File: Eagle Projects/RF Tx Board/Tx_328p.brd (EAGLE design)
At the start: 216.8 x 165.1 mm, 46 parts, among them Q3 16MHz, Q4 16MHz, U1 ATMEGA328P_TQFP, U2 MCP2551

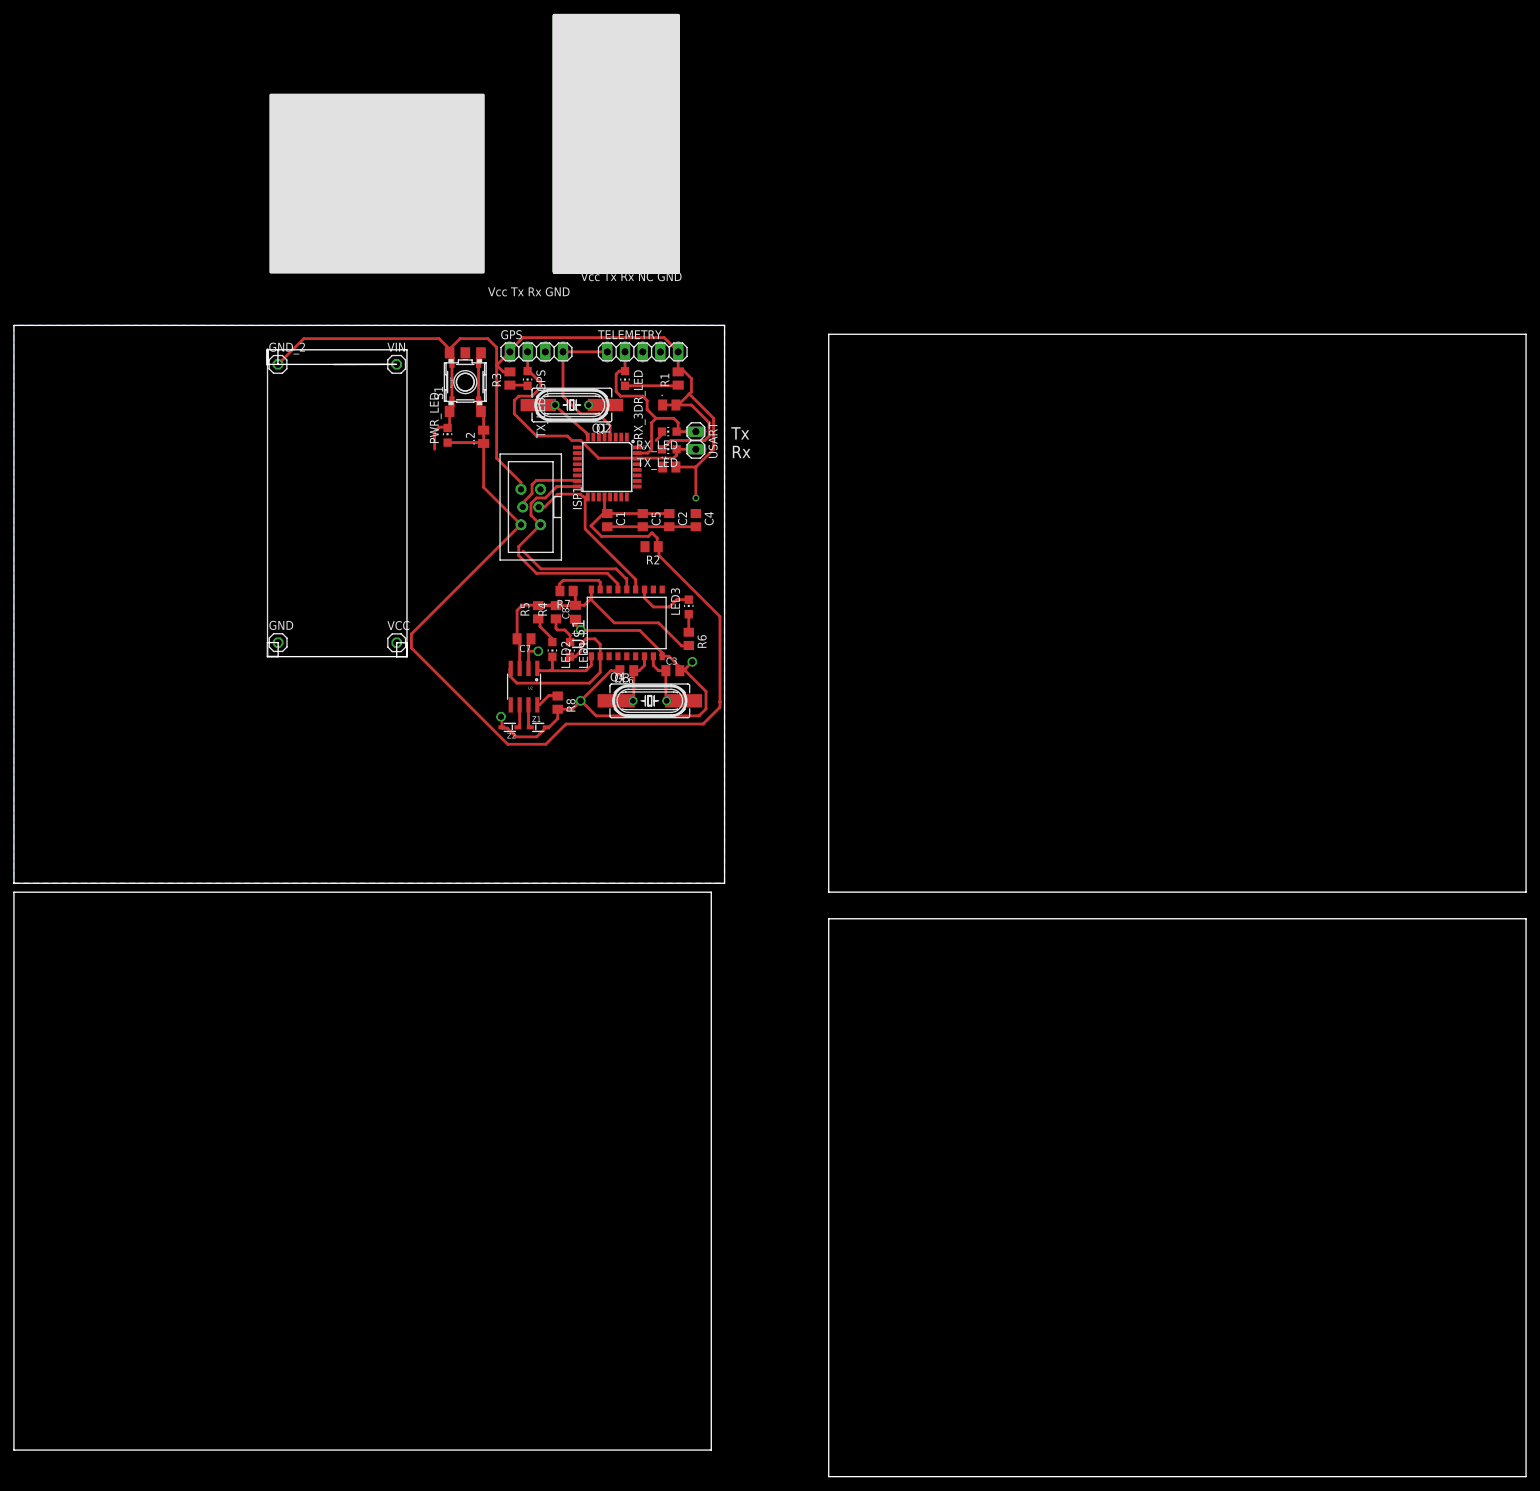
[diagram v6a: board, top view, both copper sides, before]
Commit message: Tidy up both boards
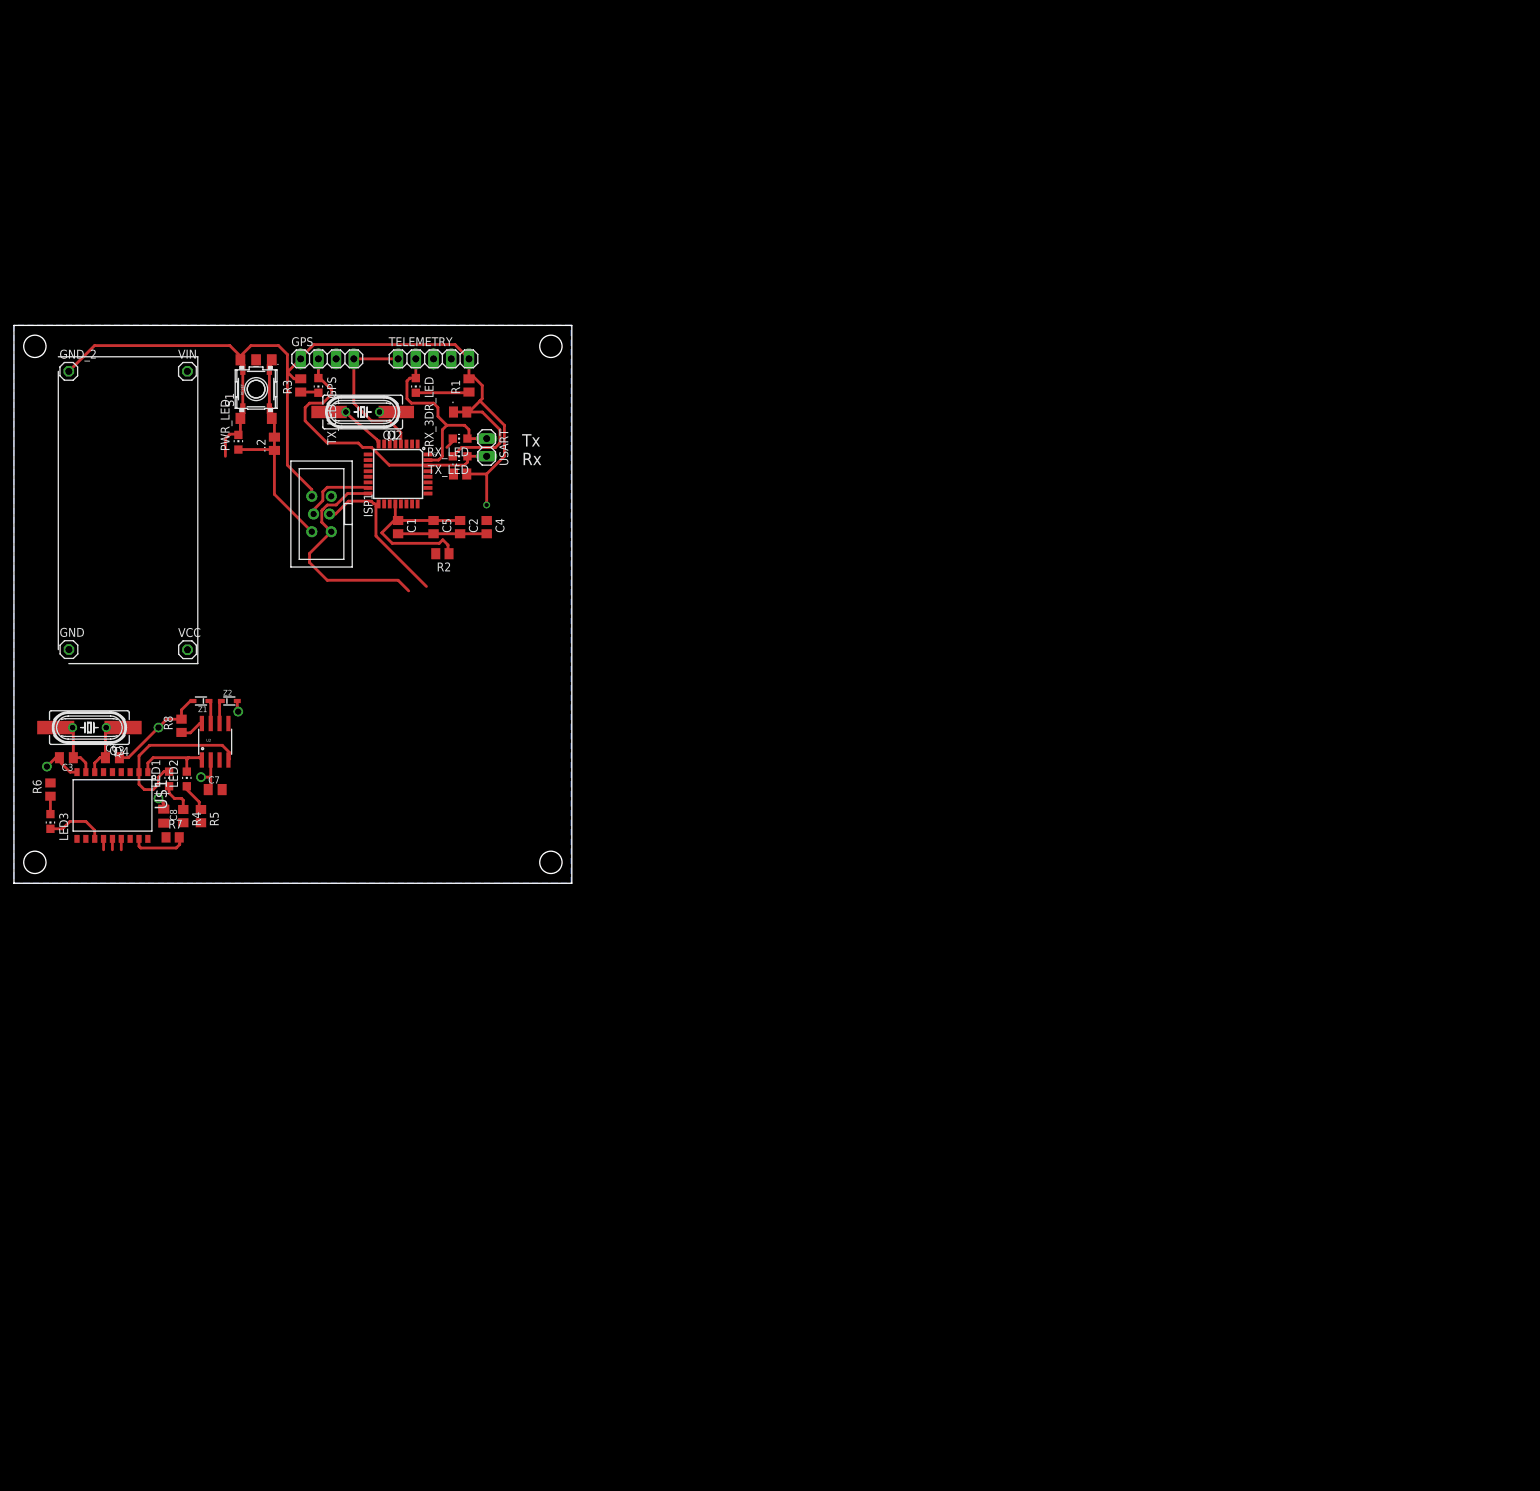
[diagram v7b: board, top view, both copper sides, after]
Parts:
- moved LED3 96.6 mm to (5.23, 8.86), turned to 180 degrees
- moved R6 94.1 mm to (5.23, 13.4), turned to 90 degrees
- moved C3 87.9 mm to (7.52, 18.0), turned to 180 degrees
- moved Q3 80.5 mm to (10.8, 22.3), turned to 180 degrees
- moved Q4 80.5 mm to (10.8, 22.3), turned to 180 degrees
- moved U$1 78.3 mm to (14.1, 11.2), turned to 180 degrees
- moved C6 74.8 mm to (14.1, 18.0), turned to 0 degrees
- moved R7 66.6 mm to (22.8, 6.58), turned to 0 degrees
- moved C8 65.9 mm to (21.5, 9.63), turned to 270 degrees
- moved R4 60.9 mm to (24.3, 9.63), turned to 270 degrees
- moved LED1 60.4 mm to (22.3, 15.0), turned to 0 degrees
- moved R5 56.5 mm to (26.8, 9.63), turned to 270 degrees
- moved LED2 55.6 mm to (24.8, 15.0), turned to 0 degrees
- moved R8 54.1 mm to (24.0, 22.6), turned to 90 degrees
- moved C7 49.3 mm to (28.9, 13.4), turned to 0 degrees
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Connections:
- net +5V: no longer C7.2, C8.2, R4.2, R5.2, R6.2, U$1.18, U2.3
- net VCC: now also C7.2, C8.2, R4.2, R5.2, R6.2, U$1.18, U2.3
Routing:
- net VCC: track 180.5 -> 77.4 mm
- net GND: track 227.6 -> 179.5 mm
- net +5V: track 44.2 -> 0.45 mm
- net MOSI: track 28.6 -> 12.1 mm
- net MISO: track 33.7 -> 34.5 mm
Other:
- board size 216.8 x 165.1 mm -> 80 x 80 mm
- board text removed: "Vcc Tx Rx GND"
- board text removed: "Vcc Tx Rx NC GND"

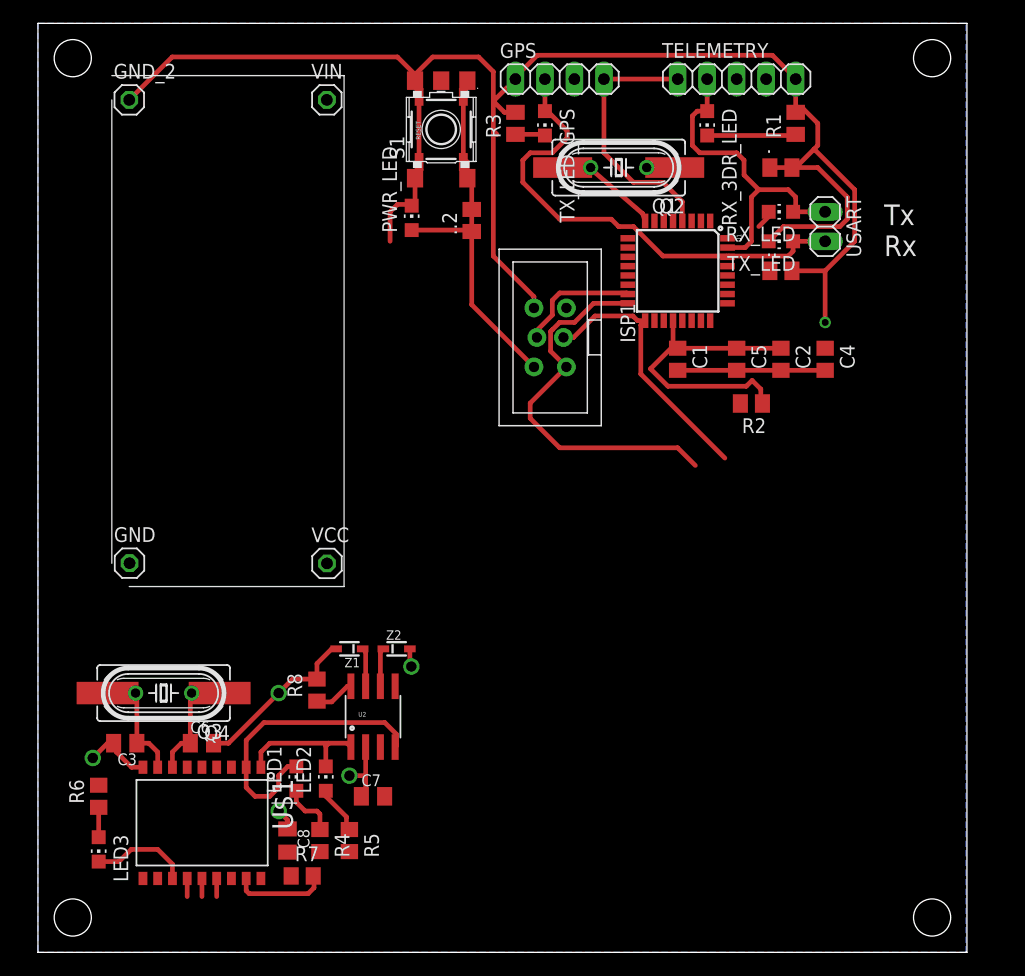
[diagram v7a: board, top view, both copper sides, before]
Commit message: More board edits, nearly done routing (actual neatness is debatable)
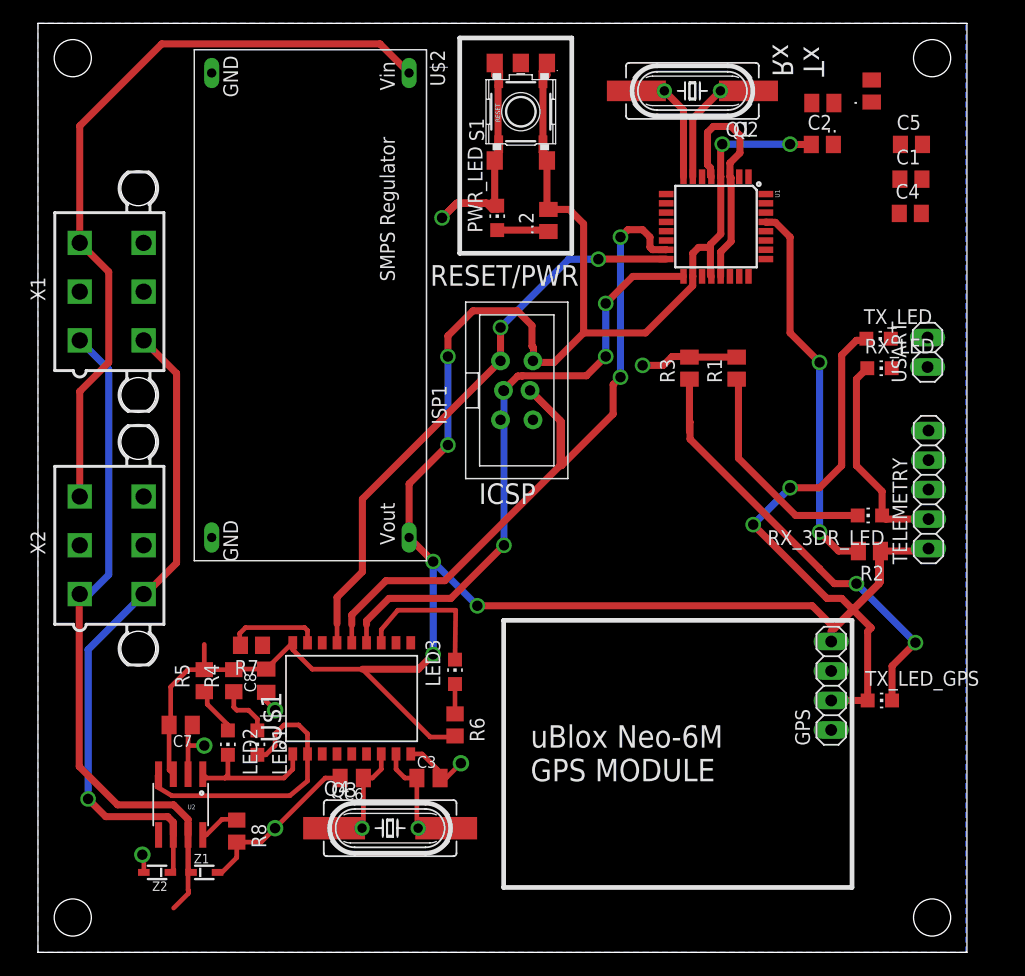
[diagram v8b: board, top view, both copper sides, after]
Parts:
- removed GND, GND_2, VCC, VIN: (no value), pinhead:1X01
- added U$2: SMPSBOARD, RobThePyro:SMPSBOARD
- added X1, X2: 5566-6, con-molex:5566-6
- moved TX_LED_GPS 57.5 mm to (72.5, 21.7), turned to 270 degrees
- moved GPS 57.2 mm to (68.3, 23.0), turned to 90 degrees
- moved TELEMETRY 39.0 mm to (76.7, 39.9), turned to 90 degrees
- moved RX_3DR_LED 36.6 mm to (71.6, 37.6), turned to 90 degrees
- moved LED3 34.3 mm to (35.9, 24.2), turned to 0 degrees
- moved R6 31.3 mm to (35.9, 19.6), turned to 270 degrees
- moved Z2 28.2 mm to (10.3, 6.88), turned to 180 degrees
- moved C3 26.3 mm to (33.6, 15.0), turned to 0 degrees
- moved R3 25.9 mm to (56.1, 50.3)
- moved C1 25.4 mm to (75.2, 66.6), turned to 0 degrees
- moved C5 23.9 mm to (75.2, 69.6), turned to 0 degrees
- moved Z1 23.0 mm to (14.3, 6.88), turned to 0 degrees
- moved Q3 22.7 mm to (30.3, 10.7), turned to 0 degrees
- moved Q4 22.7 mm to (30.3, 10.7), turned to 0 degrees
- moved R1 21.7 mm to (60.2, 50.3)
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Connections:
- new net N$20: X1.5
- new net N$21: X1.6
- new net N$26: X2.5
- new net N$27: X2.6
- new net VIN: U$2.VIN, X1.3, X2.3
- net CANH: now also X1.1, X2.1
- net CANL: now also X1.4, X2.4
- net GND: now also U$2.GND, U$2.GND@, X1.2, X2.2; no longer GND.1, GND_2.1
- net VCC: now also U$2.VOUT; no longer VCC.1
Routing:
- net VCC: track 77.4 -> 213.6 mm, vias 0 -> 7
- net GND: track 179.5 -> 61.7 mm, vias 6 -> 7
- net VIN: track 0.00 -> 66.3 mm
- net CANH: track 3.33 -> 62.0 mm
- net MOSI: track 12.1 -> 68.0 mm, vias 0 -> 2
- net CANL: track 3.33 -> 56.5 mm, vias 0 -> 1
- net N$4: track 2.58 -> 38.5 mm, vias 0 -> 2
- net N$3: track 0.00 -> 33.1 mm, vias 0 -> 2
- net SCK: track 24.5 -> 52.0 mm, vias 0 -> 4
- net N$9: track 0.00 -> 20.2 mm
- net N$8: track 17.2 -> 0.00 mm
- net MISO: track 34.5 -> 49.7 mm, vias 0 -> 2
- net N$5: track 7.66 -> 19.2 mm
- net TX0: track 29.3 -> 18.1 mm
- net N$1: track 2.41 -> 8.38 mm
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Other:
- outline, holes or cut-outs redrawn
- board text added: "ICSP"
- board text added: "RESET/PWR"
- board text added: "uBlox Neo-6M GPS MODULE"
